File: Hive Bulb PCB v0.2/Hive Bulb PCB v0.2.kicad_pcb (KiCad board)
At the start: 2 copper layers, 44.5 x 70 mm, 48 parts, among them J1 Conn_01x02, J2 USB_B_Micro, U1 NCP1117-3.3_SOT223, U2 W25Q40CLSNIG, U3 RP2040, Y1 ABLS-12.000MHZ-B4-T

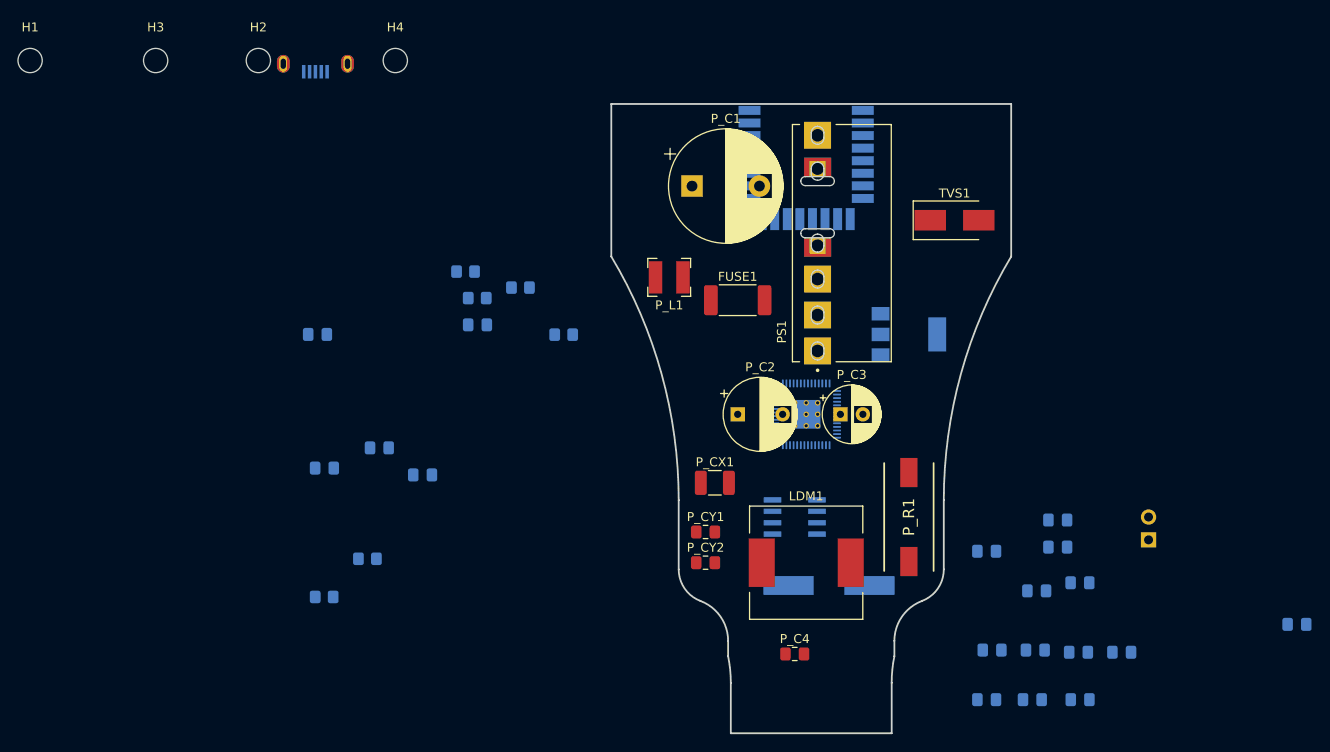
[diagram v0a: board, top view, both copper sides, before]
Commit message: Finished majority of component placement of Hive Bulb PCB v0.2.
Routing traces to come next.  Schematic still needs to be lightly adjusted.
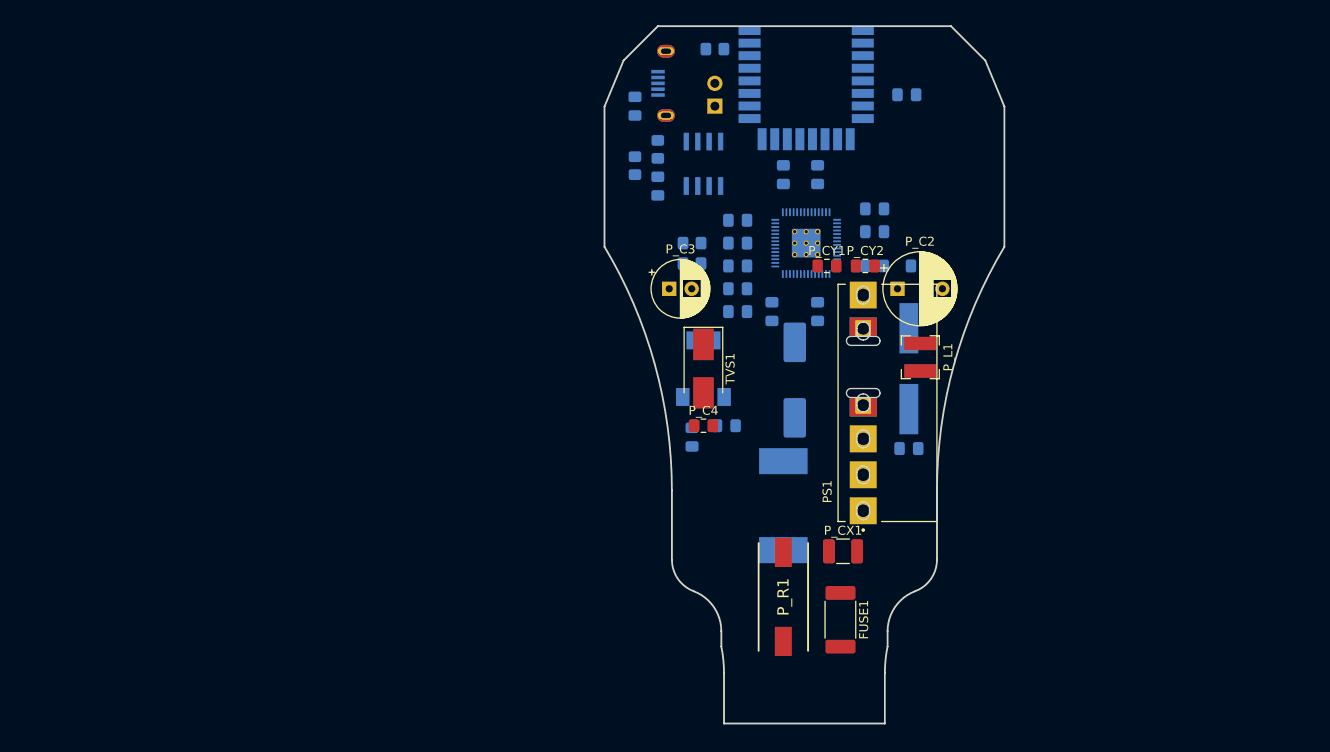
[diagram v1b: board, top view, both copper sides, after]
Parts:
- removed H1, H2, H3, H4: MountingHole, MountingHole:MountingHole_2.7mm_M2.5
- LDM1: moved to B.Cu
- P_C1: value 22uF -> 10uF; footprint Capacitor_THT:CP_Radial_D12.5mm_P7.50mm -> Capacitor_SMD:CP_Elec_10x14.3; moved to B.Cu
- moved R2 71.5 mm to (154.9, 86.4)
- moved R6 68.6 mm to (137.2, 62.2)
- moved J1 68.2 mm to (137.2, 68.6)
- moved C2 67.0 mm to (158.8, 106.7), turned to 180 degrees
- moved C6 66.6 mm to (130.8, 77.5), turned to 270 degrees
- moved C12 65.3 mm to (148.6, 76.2), turned to 90 degrees
- moved C14 63.7 mm to (148.6, 91.4), turned to 270 degrees
- moved C1 63.5 mm to (160.0, 86.4)
- moved C10 62.6 mm to (144.8, 76.2), turned to 90 degrees
- moved C17 55.6 mm to (139.7, 81.3), turned to 180 degrees
- moved C7 54.9 mm to (154.9, 82.5)
- moved C15 54.3 mm to (143.5, 91.4), turned to 270 degrees
- moved C16 53.6 mm to (139.7, 91.4), turned to 180 degrees
- moved C3 53.1 mm to (128.3, 68.6), turned to 270 degrees
- moved C18 50.2 mm to (158.5, 67.3)
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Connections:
- net /GPIO14 renamed LED_DATA_L
- U3 pad 11: /GPIO8 -> MISO
- U3 pad 12: /GPIO9 -> CS_DWM1000
- U3 pad 13: /GPIO10 -> SCK
- U3 pad 14: /GPIO11 -> MOSI
- U3 pad 15: /GPIO12 -> IRQ_DWM1000
- U3 pad 16: /GPIO13 -> RSTn_DWM1000
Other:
- board size 44.5 x 70 mm -> 44.5 x 77.6 mm

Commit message: Made testing changes to Hive Software V0.1.
Code still does not work with Hive PCB v0.1.  Most likely due to PCB design issues.  Not software.
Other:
- net class 0.15 added: clearance 0.15, trace_width 0.2, via_dia 0.6, via_drill 0.35
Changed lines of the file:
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@@
   )
   (setup
-    (last_trace_width 0.25)
+    (last_trace_width 0.2)
+    (user_trace_width 0.2)
+    (user_trace_width 0.4)
+    (user_trace_width 0.6)
+    (user_trace_width 0.8)
+    (user_trace_width 1)
     (trace_clearance 0.2)
     (zone_clearance 0.508)
@@
     (add_net VBUS)
   )
+  (net_class 0.15 ""
+    (clearance 0.15)
+    (trace_width 0.2)
+    (via_dia 0.6)
+    (via_drill 0.35)
+    (uvia_dia 0.3)
+    (uvia_drill 0.1)
+  )
   (module Capacitor_SMD:C_0805_2012Metric_Pad1.18x1.45mm_HandSolder (layer B.Cu)
     (at 160.02 86.36)
@@
       (effects (font (size 1 1) (thickness 0.15)) (justify mirror))
     )
-    (fp_line (start -1 -0.625) (end -1 0.625) (layer B.Fab) (width 0.1))
-    (fp_line (start -1 0.625) (end 1 0.625) (layer B.Fab) (width 0.1))
-    (fp_line (start 1 0.625) (end 1 -0.625) (layer B.Fab) (width 0.1))
-    (fp_line (start 1 -0.625) (end -1 -0.625) (layer B.Fab) (width 0.1))
-    (fp_line (start -0.261252 0.735) (end 0.261252 0.735) (layer B.SilkS) (width 0.12))
-    (fp_line (start -0.261252 -0.735) (end 0.261252 -0.735) (layer B.SilkS) (width 0.12))
-    (fp_line (start -1.88 -0.98) (end -1.88 0.98) (layer B.CrtYd) (width 0.05))
-    (fp_line (start -1.88 0.98) (end 1.88 0.98) (layer B.CrtYd) (width 0.05))
-    (fp_line (start 1.88 0.98) (end 1.88 -0.98) (layer B.CrtYd) (width 0.05))
-    (fp_line (start 1.88 -0.98) (end -1.88 -0.98) (layer B.CrtYd) (width 0.05))
     (fp_text user %R (at 0 0 90) (layer B.Fab)
       (effects (font (size 0.5 0.5) (thickness 0.08)) (justify mirror))
     )
-    (pad 1 smd roundrect (at -1.0375 0 270) (size 1.175 1.45) (layers B.Cu B.Paste B.Mask) (roundrect_rratio 0.212766)
-      (net 2 GND))
+    (fp_line (start 1.88 -0.98) (end -1.88 -0.98) (layer B.CrtYd) (width 0.05))
+    (fp_line (start 1.88 0.98) (end 1.88 -0.98) (layer B.CrtYd) (width 0.05))
+    (fp_line (start -1.88 0.98) (end 1.88 0.98) (layer B.CrtYd) (width 0.05))
+    (fp_line (start -1.88 -0.98) (end -1.88 0.98) (layer B.CrtYd) (width 0.05))
+    (fp_line (start -0.261252 -0.735) (end 0.261252 -0.735) (layer B.SilkS) (width 0.12))
+    (fp_line (start -0.261252 0.735) (end 0.261252 0.735) (layer B.SilkS) (width 0.12))
+    (fp_line (start 1 -0.625) (end -1 -0.625) (layer B.Fab) (width 0.1))
+    (fp_line (start 1 0.625) (end 1 -0.625) (layer B.Fab) (width 0.1))
+    (fp_line (start -1 0.625) (end 1 0.625) (layer B.Fab) (width 0.1))
+    (fp_line (start -1 -0.625) (end -1 0.625) (layer B.Fab) (width 0.1))
     (pad 2 smd roundrect (at 1.0375 0 270) (size 1.175 1.45) (layers B.Cu B.Paste B.Mask) (roundrect_rratio 0.212766)
       (net 4 "Net-(C3-Pad2)"))
+    (pad 1 smd roundrect (at -1.0375 0 270) (size 1.175 1.45) (layers B.Cu B.Paste B.Mask) (roundrect_rratio 0.212766)
+      (net 2 GND))
     (model ${KISYS3DMOD}/Capacitor_SMD.3dshapes/C_0805_2012Metric.wrl
       (at (xyz 0 0 0))
@@
       (effects (font (size 1 1) (thickness 0.15)) (justify mirror))
     )
-    (fp_line (start -1 -0.625) (end -1 0.625) (layer B.Fab) (width 0.1))
-    (fp_line (start -1 0.625) (end 1 0.625) (layer B.Fab) (width 0.1))
-    (fp_line (start 1 0.625) (end 1 -0.625) (layer B.Fab) (width 0.1))
-    (fp_line (start 1 -0.625) (end -1 -0.625) (layer B.Fab) (width 0.1))
-    (fp_line (start -0.227064 0.735) (end 0.227064 0.735) (layer B.SilkS) (width 0.12))
-    (fp_line (start -0.227064 -0.735) (end 0.227064 -0.735) (layer B.SilkS) (width 0.12))
-    (fp_line (start -1.85 -0.95) (end -1.85 0.95) (layer B.CrtYd) (width 0.05))
-    (fp_line (start -1.85 0.95) (end 1.85 0.95) (layer B.CrtYd) (width 0.05))
-    (fp_line (start 1.85 0.95) (end 1.85 -0.95) (layer B.CrtYd) (width 0.05))
-    (fp_line (start 1.85 -0.95) (end -1.85 -0.95) (layer B.CrtYd) (width 0.05))
     (fp_text user %R (at 0 0) (layer B.Fab)
       (effects (font (size 0.5 0.5) (thickness 0.08)) (justify mirror))
     )
-    (pad 1 smd roundrect (at -1 0) (size 1.2 1.4) (layers B.Cu B.Paste B.Mask) (roundrect_rratio 0.208333)
-      (net 2 GND))
+    (fp_line (start 1.85 -0.95) (end -1.85 -0.95) (layer B.CrtYd) (width 0.05))
+    (fp_line (start 1.85 0.95) (end 1.85 -0.95) (layer B.CrtYd) (width 0.05))
+    (fp_line (start -1.85 0.95) (end 1.85 0.95) (layer B.CrtYd) (width 0.05))
+    (fp_line (start -1.85 -0.95) (end -1.85 0.95) (layer B.CrtYd) (width 0.05))
+    (fp_line (start -0.227064 -0.735) (end 0.227064 -0.735) (layer B.SilkS) (width 0.12))
+    (fp_line (start -0.227064 0.735) (end 0.227064 0.735) (layer B.SilkS) (width 0.12))
+    (fp_line (start 1 -0.625) (end -1 -0.625) (layer B.Fab) (width 0.1))
+    (fp_line (start 1 0.625) (end 1 -0.625) (layer B.Fab) (width 0.1))
+    (fp_line (start -1 0.625) (end 1 0.625) (layer B.Fab) (width 0.1))
+    (fp_line (start -1 -0.625) (end -1 0.625) (layer B.Fab) (width 0.1))
     (pad 2 smd roundrect (at 1 0) (size 1.2 1.4) (layers B.Cu B.Paste B.Mask) (roundrect_rratio 0.208333)
       (net 25 IRQ_DWM1000))
+    (pad 1 smd roundrect (at -1 0) (size 1.2 1.4) (layers B.Cu B.Paste B.Mask) (roundrect_rratio 0.208333)
+      (net 2 GND))
     (model ${KISYS3DMOD}/Resistor_SMD.3dshapes/R_0805_2012Metric.wrl
       (at (xyz 0 0 0))
